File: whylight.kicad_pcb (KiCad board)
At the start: 4 copper layers, 107.9 x 40 mm, 92 parts, among them J1 USB device, J2 External 5v, J3 External 5v, J4 I2C, J5 UART, J7 Ledstrip, U1 AG5405, U10 INA233, U11 L78L05_SOT89, U2 KPC357NT0ATLD, U3 ESP32-C6-WROOM-1, U4 Ra-01SH, U5 W5500, U6 AP63203WU, U7 USBLC6-2P6, U8 74LVC1G125, U9 74LVC1G125, Y1 25MHz

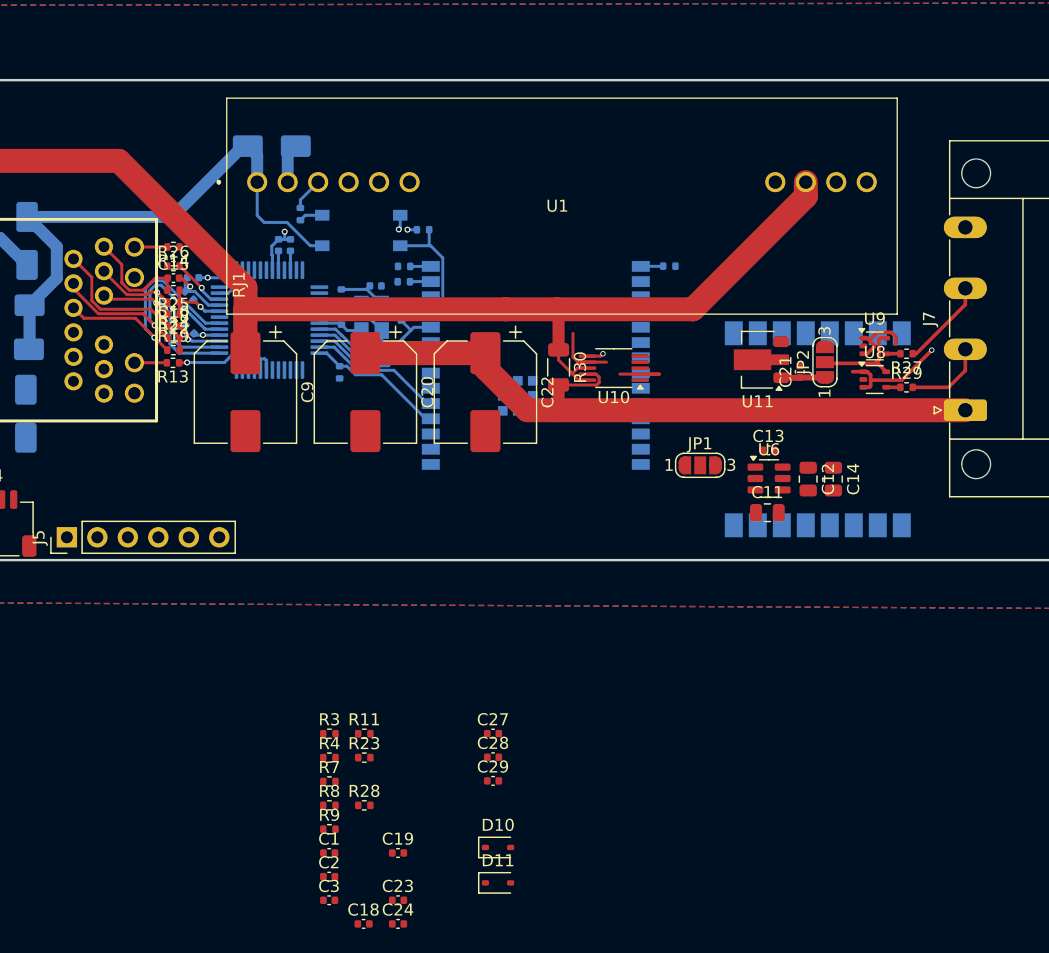
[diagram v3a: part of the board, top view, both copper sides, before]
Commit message: added 3D models, added LCSC numbers, added caps in RX line ethernet as per the datasheet, change crystal and capacitors to correctly match w5500 as per the datasheet, added bead to filter analoge power supply for w5500 as per the datasheet, added filter for the ina2XX for beter monitoring
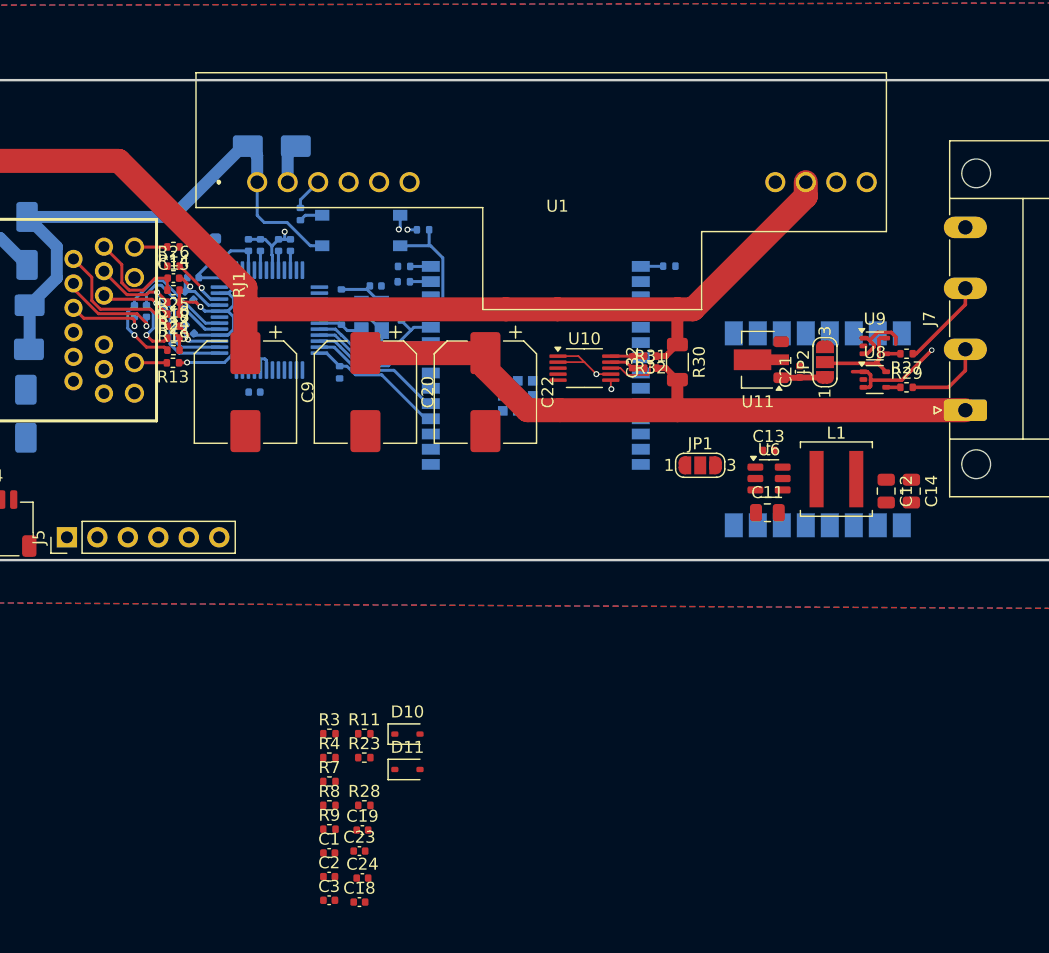
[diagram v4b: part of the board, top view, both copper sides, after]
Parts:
- added C30: 6.8n, Capacitor_SMD:C_0402_1005Metric, B.Cu at (30.8, -0.75)
- added C31: 6.8n, Capacitor_SMD:C_0402_1005Metric, B.Cu at (31.8, -0.75)
- added C32: 100n, Capacitor_SMD:C_0402_1005Metric, F.Cu at (72.2, 3.52)
- added FB1: 120, Inductor_SMD:L_0603_1608Metric, B.Cu at (37.5, -6.00)
- added L1: 3.9u, Inductor_SMD:L_Coilcraft_XAL5050-XXX, F.Cu at (89.2, 13.2)
- added R31: 10, Resistor_SMD:R_0402_1005Metric, F.Cu at (73.8, 3.00)
- added R32: 10, Resistor_SMD:R_0402_1005Metric, F.Cu at (73.8, 4.00)
- C27, C28, C29: moved to B.Cu
- C4, C8: value 22p -> 18p
- moved C28 46.9 mm to (41.2, -6.25), turned to 90 degrees
- moved C27 45.5 mm to (40.2, -6.25), turned to 90 degrees
- moved C29 38.0 mm to (40.8, 6.00), turned to 180 degrees
- moved D10 12.1 mm to (53.5, 34.5)
- moved D11 12.1 mm to (53.5, 37.5)
- moved R30 9.91 mm to (76.0, 3.50)
- moved C12 6.58 mm to (93.4, 14.2)
- moved C14 6.58 mm to (95.5, 14.2)
- moved C23 5.21 mm to (49.5, 44.2)
- moved C24 4.84 mm to (49.8, 46.5)
- moved C19 3.53 mm to (49.8, 42.5)
- moved U10 2.45 mm to (68.2, 4.00), turned to 0 degrees
- moved C18 1.85 mm to (49.5, 48.5)
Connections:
- C25 pad 1: +3.3V -> VDDA
- C26 pad 1: +3.3V -> VDDA
- C27 pad 1: +3.3V -> VDDA
- C28 pad 1: +3.3V -> VDDA
- C5 pad 1: +3.3V -> VDDA
- R19 pad 1: /Ethernet/ETH_RX_P -> Net-(U5-RXP)
- R24 pad 1: /Ethernet/ETH_RX_N -> Net-(U5-RXN)
- U10 pad 10: +VIN -> Net-(U10-Vin+)
- U10 pad 9: VLED -> Net-(U10-Vin-)
- U5 pad 11: +3.3V -> VDDA
- U5 pad 15: +3.3V -> VDDA
- U5 pad 17: +3.3V -> VDDA
- U5 pad 21: +3.3V -> VDDA
- U5 pad 4: +3.3V -> VDDA
- U5 pad 5: /Ethernet/ETH_RX_N -> Net-(U5-RXN)
- U5 pad 6: /Ethernet/ETH_RX_P -> Net-(U5-RXP)
- U5 pad 8: +3.3V -> VDDA
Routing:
- net VDDA: track 0.00 -> 20.4 mm
- net Net-(U5-RXP): track 0.00 -> 15.9 mm, vias 0 -> 1
- net /Ethernet/ETH_RX_P: track 21.6 -> 6.77 mm
- net Net-(U5-RXN): track 0.00 -> 13.8 mm, vias 0 -> 1
- net /Ethernet/ETH_RX_N: track 20.1 -> 8.37 mm
- net +3.3V: track 19.0 -> 11.7 mm, vias 5 -> 3
- net Net-(U10-Vin-): track 0.00 -> 3.00 mm
- net Net-(U10-Vin+): track 0.00 -> 2.82 mm
- net VLED: track 59.9 -> 57.5 mm
- net +VIN: track 119.8 -> 121.4 mm
- net /Ethernet/ETH_LED1: track 15.9 -> 15.2 mm
- net GND: track 75.2 -> 74.8 mm, vias 11 -> 12

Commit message: Change pinout of C6 to more closely resemble the WHY2025 badge
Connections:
- U3 pad 19: LORA_BUSY -> ETH_INT
- U3 pad 20: LORA_DIO1 -> ETH_LED2B
- U3 pad 23: LORA_CS -> ALERT
- U3 pad 26: ALERT -> SPI_MISO
- U3 pad 27: ETH_LED2B -> SPI_MOSI
- U3 pad 4: ETH_INT -> LORA_DIO1
- U3 pad 5: SPI_MOSI -> LORA_BUSY
- U3 pad 8: SPI_MISO -> SPI_SCK
- U3 pad 9: SPI_SCK -> LORA_CS

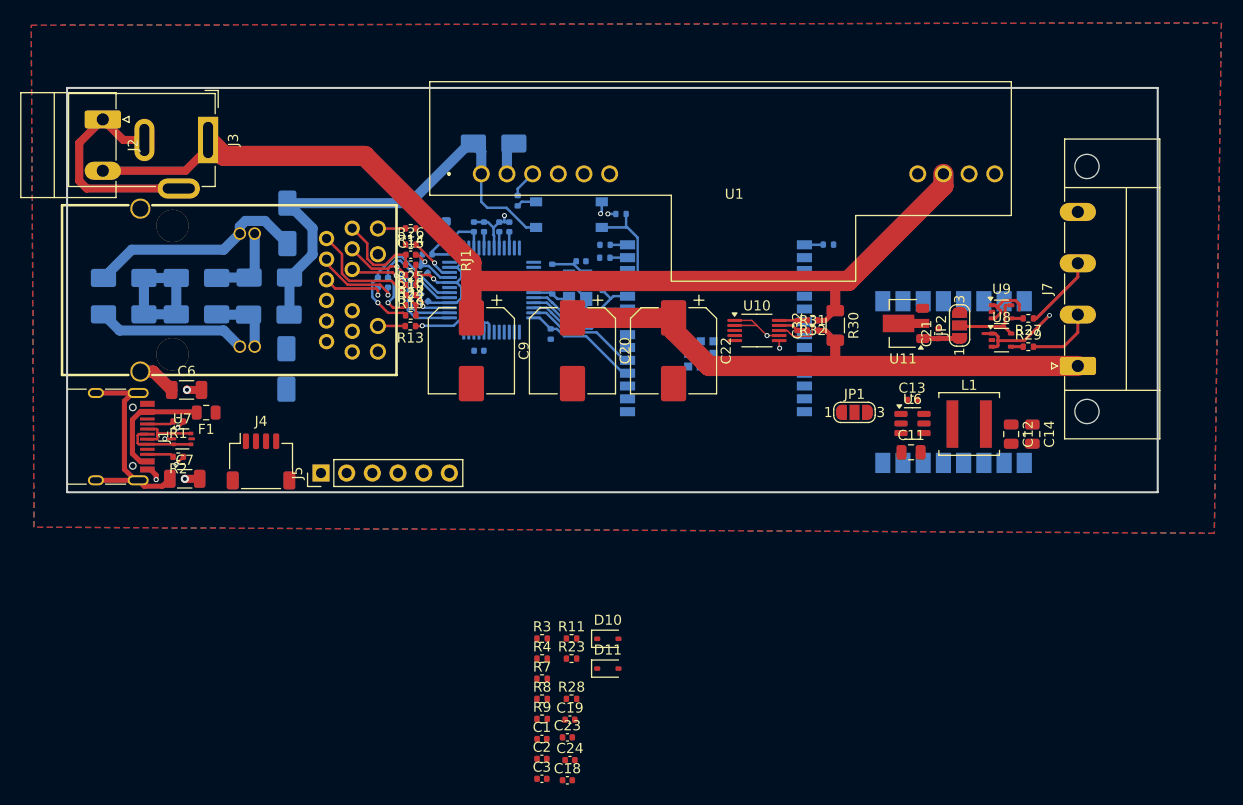
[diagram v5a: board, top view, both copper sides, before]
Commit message: Add RS485, add mounting holes, route more stuff
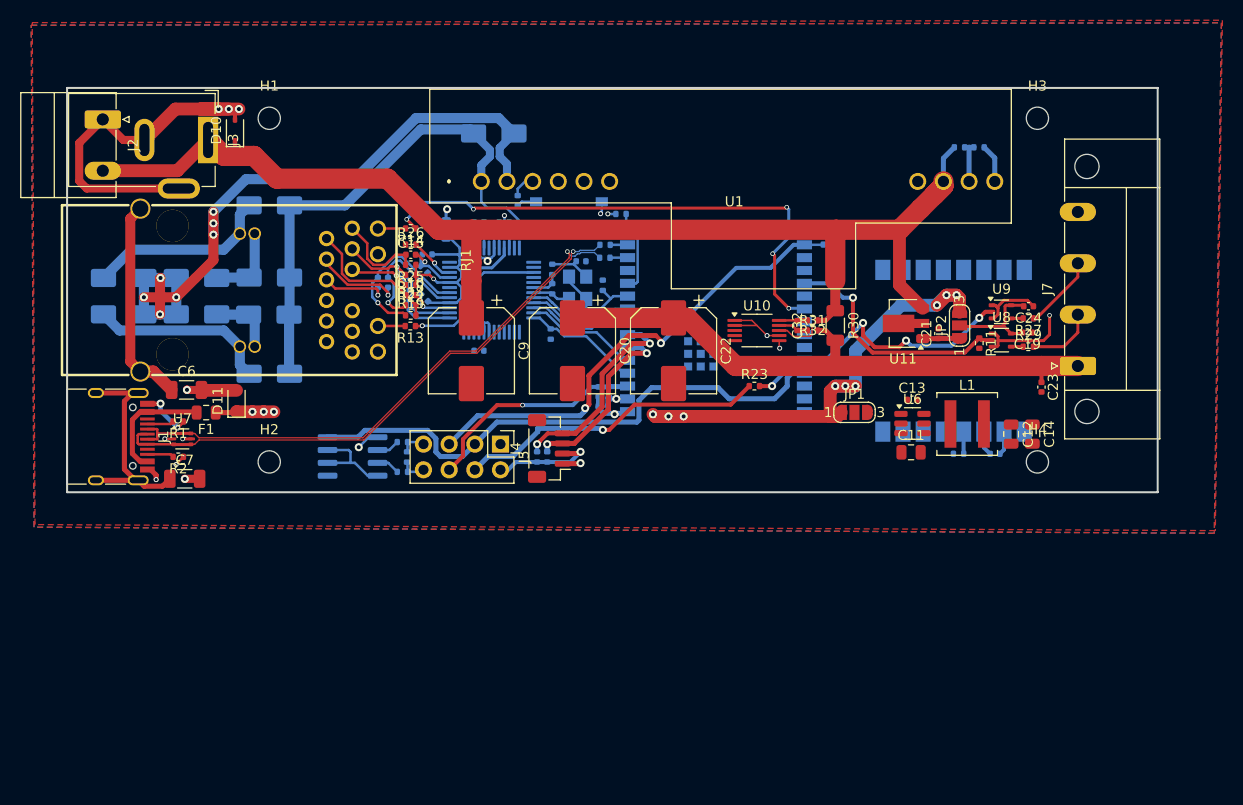
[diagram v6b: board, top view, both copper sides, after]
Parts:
- added H1: ~, MountingHole:MountingHole_2.2mm_M2, F.Cu at (20.0, -17.0)
- added H2: ~, MountingHole:MountingHole_2.2mm_M2, F.Cu at (20.0, 17.0)
- added H3: ~, MountingHole:MountingHole_2.2mm_M2, F.Cu at (96.0, -17.0)
- added H4: ~, MountingHole:MountingHole_2.2mm_M2, F.Cu at (96.0, 17.0)
- added R33: 22, Resistor_SMD:R_0402_1005Metric, B.Cu at (33.2, 15.0)
- added R34: 22, Resistor_SMD:R_0402_1005Metric, B.Cu at (33.2, 18.0)
- added R35: 120, Resistor_SMD:R_0402_1005Metric, B.Cu at (33.6, 16.5)
- added U12: GM3085N, Package_SO:SOIC-8_3.9x4.9mm_P1.27mm, B.Cu at (28.2, 16.5)
- C1, C18, C2, C3, R28, R3, R4, R7, R8, R9: moved to B.Cu
- J4: footprint Connector_JST:JST_SH_SM04B-SRSS-TB_1x04-1MP_P1.00mm_Horizontal -> Connector_JST:JST_SH_BM04B-SRSS-TB_1x04-1MP_P1.00mm_Vertical
- J5: footprint Connector_PinHeader_2.54mm:PinHeader_1x06_P2.54mm_Vertical -> Connector_PinHeader_2.54mm:PinHeader_2x04_P2.54mm_Vertical
- moved R4 66.5 mm to (90.2, -14.1), turned to 180 degrees
- moved C24 63.8 mm to (95.1, 1.60), turned to 180 degrees
- moved R3 63.8 mm to (88.3, -14.1), turned to 180 degrees
- moved D10 62.4 mm to (16.6, -15.8), turned to 90 degrees
- moved C3 61.7 mm to (42.3, -13.2)
- moved C19 59.3 mm to (95.0, 4.20), turned to 180 degrees
- moved C23 58.3 mm to (96.4, 9.60), turned to -90 degrees
- moved C18 53.2 mm to (91.8, 16.2)
- moved R11 49.8 mm to (90.2, 5.25), turned to -90 degrees
- moved R28 45.3 mm to (88.2, 16.2), turned to 180 degrees
- moved D11 45.3 mm to (16.8, 11.0), turned to 90 degrees
- moved C2 36.8 mm to (52.6, 10.1), turned to -90 degrees
- moved C1 33.5 mm to (53.0, 11.5), turned to 180 degrees
- moved R23 32.5 mm to (68.0, 9.50)
- moved R7 29.1 mm to (53.6, 10.1), turned to 90 degrees
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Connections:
- R11 pad 1: ETH_LED2A -> LDAT
- R18 pad 1: +3.3V -> VDDA
- R22 pad 1: +3.3V -> VDDA
- R25 pad 1: +3.3V -> VDDA
- U3 pad 19: ETH_INT -> LORA_DIO1
- U3 pad 26: SPI_MISO -> LORA_CS
- U3 pad 27: SPI_MOSI -> LORA_BUSY
- U3 pad 4: LORA_DIO1 -> ETH_INT
- U3 pad 5: LORA_BUSY -> SPI_MOSI
- U3 pad 8: SPI_SCK -> SPI_MISO
- U3 pad 9: LORA_CS -> SPI_SCK
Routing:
- net +5v-USB: track 0.00 -> 95.1 mm, vias 0 -> 12
- net UART_TX: track 0.00 -> 55.3 mm
- net Net-(D2-A): track 16.9 -> 71.8 mm, vias 0 -> 7
- net ETH_LED2B: track 0.00 -> 52.9 mm, vias 0 -> 5
- net USB_N: track 6.26 -> 55.7 mm, vias 0 -> 1
- net USB_P: track 7.08 -> 56.0 mm, vias 0 -> 1
- net BOOT: track 1.84 -> 47.7 mm, vias 0 -> 2
- net GND: track 74.8 -> 119.4 mm, vias 12 -> 20
- net UART_RX: track 0.00 -> 30.9 mm, vias 0 -> 1
- net LCLK: track 0.00 -> 29.3 mm, vias 0 -> 4
- net LDAT: track 0.00 -> 24.1 mm, vias 0 -> 1
- net EN: track 0.00 -> 22.1 mm, vias 0 -> 1
- net I2C_SCL: track 0.00 -> 20.5 mm, vias 0 -> 2
- net I2C_SDA: track 0.00 -> 18.4 mm, vias 0 -> 2
- net Net-(C6-Pad1): track 3.85 -> 20.8 mm
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
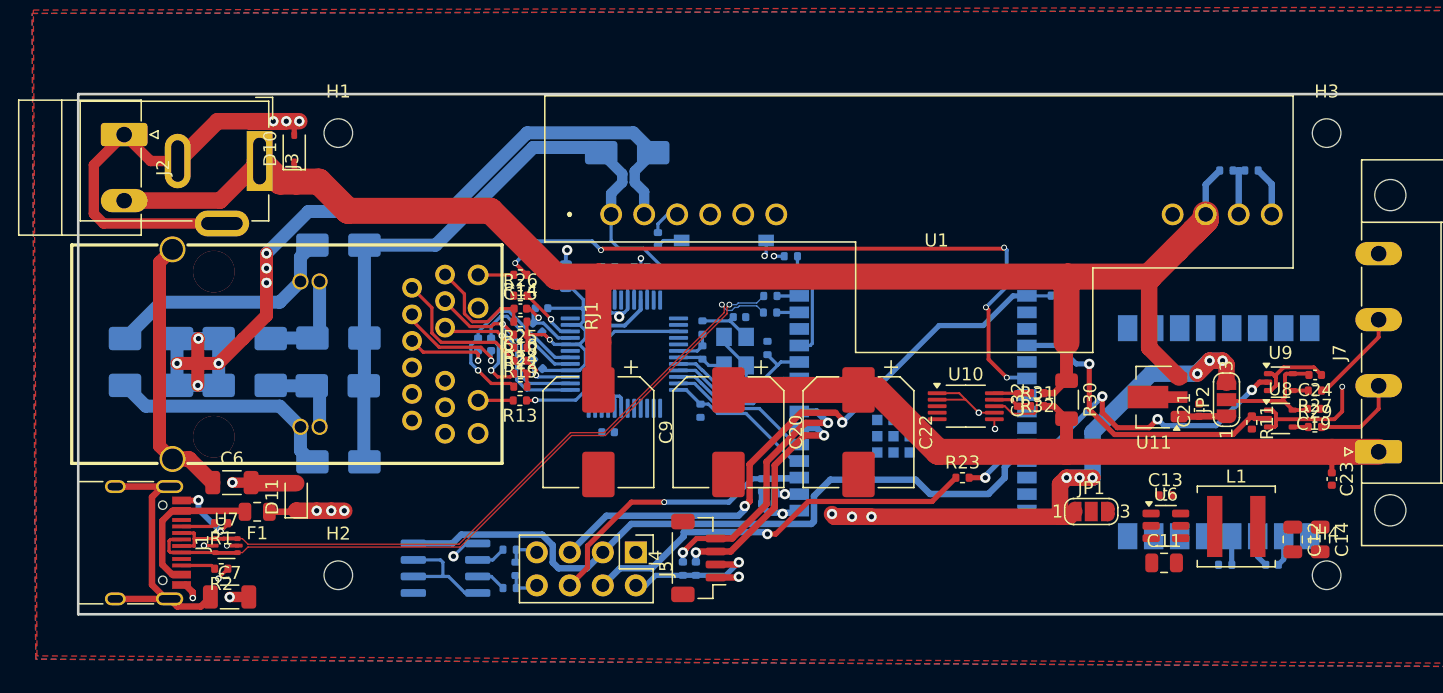
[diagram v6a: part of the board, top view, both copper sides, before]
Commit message: Finish first pass of routing
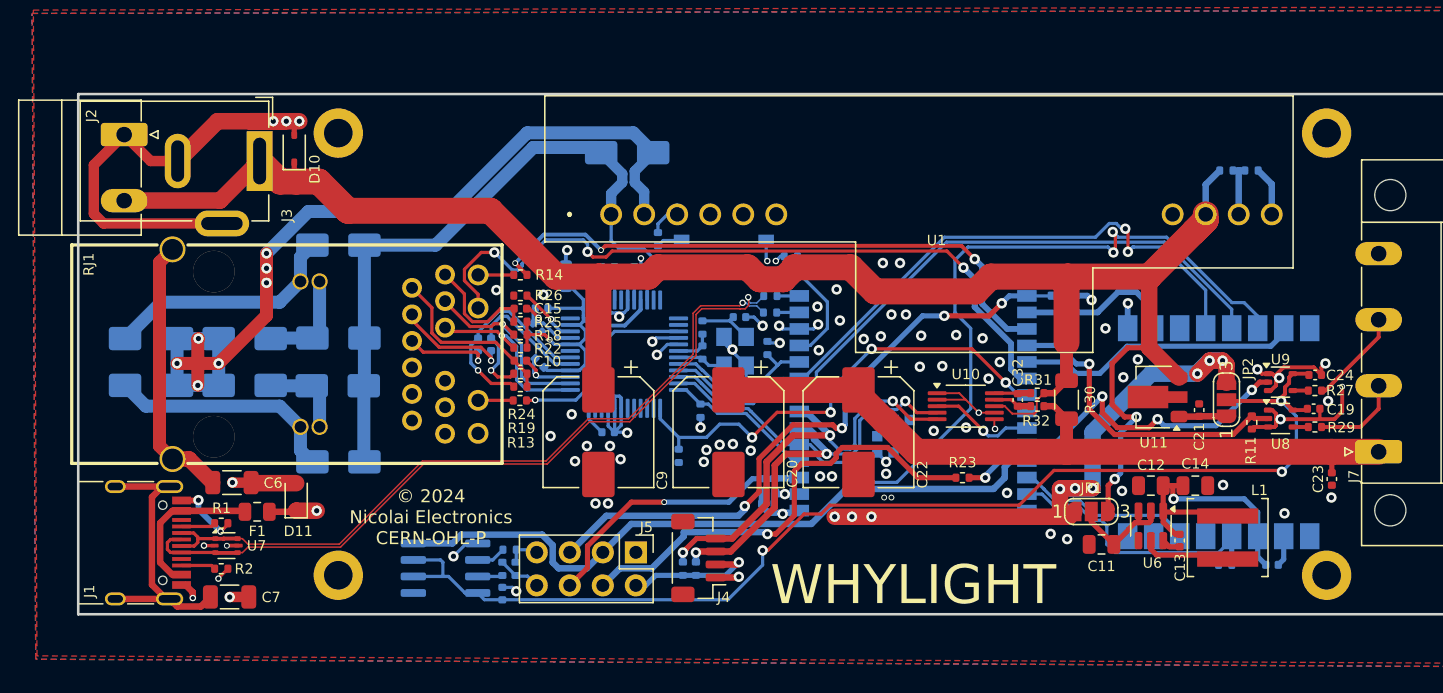
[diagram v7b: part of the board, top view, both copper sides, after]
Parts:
- added C33: 100n, Capacitor_SMD:C_0402_1005Metric, B.Cu at (32.6, 18.4)
- added R36: 51k, Resistor_SMD:R_0402_1005Metric, B.Cu at (46.2, 7.82)
- H1, H2, H3, H4: footprint MountingHole:MountingHole_2.2mm_M2 -> MountingHole:MountingHole_2.2mm_M2_DIN965_Pad
- moved C12 11.7 mm to (82.5, 10.1), turned to 180 degrees
- moved C14 10.5 mm to (85.9, 10.1), turned to 0 degrees
- moved C11 5.02 mm to (78.7, 14.6), turned to 180 degrees
- moved C13 3.65 mm to (84.7, 14.3), turned to -90 degrees
- moved R34 1.58 mm to (32.6, 16.5), turned to -90 degrees
- moved U6 1.15 mm to (82.5, 13.2), turned to -90 degrees
- moved L1 1.08 mm to (88.4, 14.1), turned to 90 degrees
- moved C5 0.15 mm to (35.5, 0.68)
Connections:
- U3 pad 16: LORA_RESET -> LORA_BUSY
- U3 pad 17: ETH_LED2A -> ETH_LED2B
- U3 pad 19: LORA_DIO1 -> LORA_CS
- U3 pad 20: ETH_LED2B -> ETH_LED2A
- U3 pad 26: LORA_CS -> LORA_DIO1
- U3 pad 27: LORA_BUSY -> LORA_RESET
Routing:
- net +5V: track 19.6 -> 92.1 mm, vias 0 -> 3
- net SPI_MOSI: track 10.9 -> 69.0 mm, vias 0 -> 2
- net ETH_LED2A: track 0.00 -> 55.9 mm, vias 0 -> 3
- net SPI_SCK: track 10.8 -> 53.0 mm, vias 0 -> 2
- net SPI_MISO: track 10.4 -> 52.3 mm
- net ETH_RESET: track 0.00 -> 36.7 mm, vias 0 -> 4
- net +3.3V: track 23.4 -> 56.9 mm, vias 6 -> 12
- net LORA_CS: track 0.00 -> 21.4 mm
- net +VIN: track 129.1 -> 148.4 mm, vias 0 -> 2
- net LORA_RESET: track 2.20 -> 21.0 mm
- net GND: track 119.4 -> 137.3 mm, vias 20 -> 82
- net LORA_DIO1: track 0.00 -> 13.1 mm
- net I2C_SCL: track 20.5 -> 33.0 mm, vias 2 -> 3
- net I2C_SDA: track 18.4 -> 30.8 mm, vias 2 -> 3
- net LORA_BUSY: track 0.00 -> 12.4 mm
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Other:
- board text added: "- c d +"
- board text added: "PoE+"
- board text added: "WHYLIGHT"
- board text added: "© 2024 Nicolai Electronics CERN-OHL-P"

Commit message: Rerouted power to where there is more space, solved issue with diff pair.
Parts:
- moved D10 9.72 mm to (26.3, -14.8)
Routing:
- net GND: track 137.3 -> 98.0 mm, vias 82 -> 81
- net +VIN: track 148.4 -> 182.2 mm
- net +3.3V: track 56.9 -> 46.6 mm
- net Net-(D2-A): track 71.8 -> 64.9 mm, vias 7 -> 8
- net USB_P: track 58.6 -> 63.4 mm
- net USB_N: track 56.7 -> 61.3 mm
- net Net-(C6-Pad1): track 20.8 -> 23.2 mm
- net ETH_LED2A: track 55.9 -> 56.5 mm
- added copper zone on B.Cu, net +3.3V
- added copper zone on F.Cu, net +VIN
- added copper zone on F.Cu, net Net-(D2-A)
